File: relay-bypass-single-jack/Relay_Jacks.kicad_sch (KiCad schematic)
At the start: 14 parts, among them J1 4, J3 4, K1 IM05JR, Q1 DMN62D0U-7, U6 TLP170AM

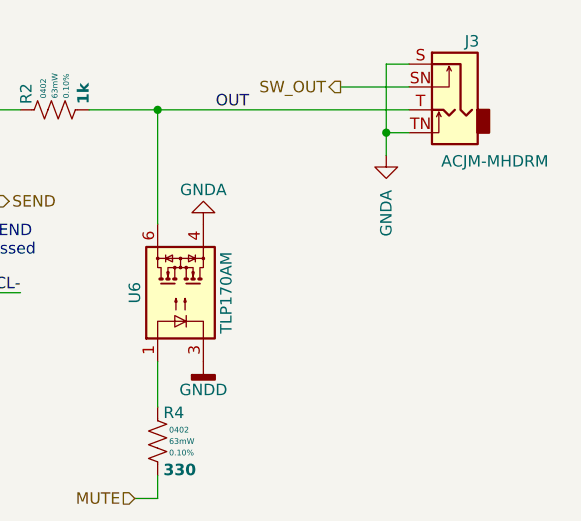
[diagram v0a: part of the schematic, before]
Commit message: Added second project for exploring a single-jack side mounted version
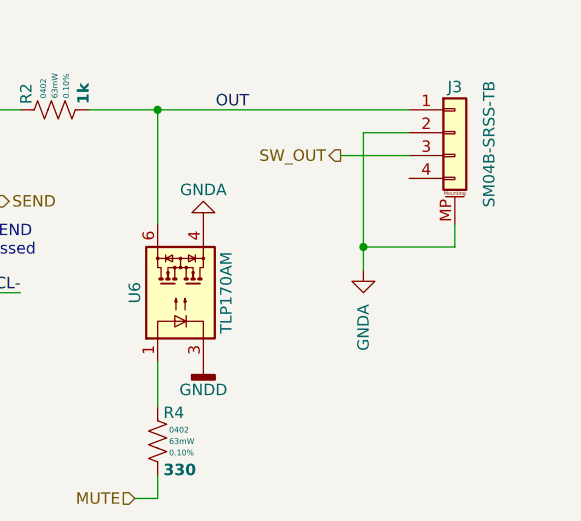
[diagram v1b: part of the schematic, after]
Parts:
- removed J3: 4, g-con:Amphenol_ACJM-MHDR(M), symbol #gplm:con/CON-1003-M301
- added J3: 4, Connector_JST:JST_SH_BM04B-SRSS-TB_1x04-1MP_P1.00mm_Vertical, symbol #gplm:con/CON-5001-0004
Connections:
- net GNDA: now also J3.2 (Pin_2), J3.MP (MountPin)
- net OUT: now also J3.1 (Pin_1)
- net SW_OUT: now also J3.3 (Pin_3)
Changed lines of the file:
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@@
 	)
 	(junction
-		(at 233.68 58.42)
-		(diameter 0)
-		(color 0 0 0 0)
-	)
-	(junction
 		(at 119.38 60.96)
 		(diameter 0)
@@
 	)
 	(junction
+		(at 231.14 71.12)
+		(diameter 0)
+		(color 0 0 0 0)
+	)
+	(junction
 		(at 152.4 76.2)
 		(diameter 0)
@@
 	(wire
 		(pts
-			(xy 233.68 60.96) (xy 233.68 58.42)
+			(xy 231.14 73.66) (xy 231.14 71.12)
 		)
 		(stroke
@@
 	(wire
 		(pts
+			(xy 241.3 68.58) (xy 241.3 71.12)
+		)
+		(stroke
+			(width 0)
+			(type default)
+		)
+	)
+	(wire
+		(pts
 			(xy 144.78 83.82) (xy 144.78 82.55)
 		)
@@
 	(wire
 		(pts
+			(xy 231.14 71.12) (xy 231.14 58.42)
+		)
+		(stroke
+			(width 0)
+			(type default)
+		)
+	)
+	(wire
+		(pts
 			(xy 163.83 116.84) (xy 170.18 116.84)
 		)
@@
 	(wire
 		(pts
-			(xy 236.22 53.34) (xy 228.6 53.34)
+			(xy 236.22 60.96) (xy 228.6 60.96)
 		)
 		(stroke
@@
 	(wire
 		(pts
-			(xy 233.68 58.42) (xy 236.22 58.42)
+			(xy 231.14 58.42) (xy 236.22 58.42)
 		)
 		(stroke
@@
 	(wire
 		(pts
-			(xy 182.88 111.76) (xy 182.88 116.84)
+			(xy 241.3 71.12) (xy 231.14 71.12)
 		)
 		(stroke
@@
 	(wire
 		(pts
-			(xy 116.84 53.34) (xy 119.38 53.34)
+			(xy 182.88 111.76) (xy 182.88 116.84)
 		)
 		(stroke
@@
 	(wire
 		(pts
-			(xy 165.1 63.5) (xy 162.56 63.5)
+			(xy 116.84 53.34) (xy 119.38 53.34)
 		)
 		(stroke
@@
 	(wire
 		(pts
-			(xy 208.28 55.88) (xy 236.22 55.88)
+			(xy 165.1 63.5) (xy 162.56 63.5)
 		)
 		(stroke
@@
 	(wire
 		(pts
-			(xy 233.68 50.8) (xy 233.68 58.42)
+			(xy 208.28 55.88) (xy 236.22 55.88)
 		)
 		(stroke
@@
 	(wire
 		(pts
-			(xy 236.22 50.8) (xy 233.68 50.8)
-		)
-		(stroke
-			(width 0)
-			(type default)
-		)
-	)
-	(wire
-		(pts
 			(xy 149.86 106.68) (xy 165.1 106.68)
 		)
@@
 	(hierarchical_label "SW_OUT"
 		(shape output)
-		(at 228.6 53.34 180)
+		(at 228.6 60.96 180)
 		(effects
 			(font
@@
 	)
 	(symbol
+		(lib_id "#gplm:con/CON-5001-0004")
+		(at 241.3 58.42 0)
+		(unit 1)
+		(exclude_from_sim no)
+		(in_bom yes)
+		(on_board yes)
+		(dnp no)
+		(property "Reference" "J3"
+			(at 241.3 53.34 0)
+			(effects
+				(font
+					(size 1.27 1.27)
+				)
+			)
+		)
+		(property "Value" "4"
+			(at 242.57 66.04 0)
+			(effects
+				(font
+					(size 1.27 1.27)
+				)
+				(justify left)
+				(hide yes)
+			)
+		)
+		(property "Footprint" "Connector_JST:JST_SH_BM04B-SRSS-TB_1x04-1MP_P1.00mm_Vertical"
+			(at 241.3 58.42 0)
+			(effects
+				(font
+					(size 1.27 1.27)
+				)
+				(hide yes)
+			)
+		)
+		(property "Datasheet" "https://www.jst.com/wp-content/uploads/2021/01/eSH-new.pdf"
+			(at 241.3 58.42 0)
+			(effects
+				(font
+					(size 1.27 1.27)
+				)
+				(hide yes)
+			)
+		)
+		(property "Description" "CONN WIRE TO BOARD SMD R/A 4POS 1MM"
+			(at 241.3 58.42 0)
+			(effects
+				(font
+					(size 1.27 1.27)
+				)
+				(hide yes)
+			)
+		)
+		(property "IPN" "CON-5001-0004"
+			(at 241.3 58.42 0)
+			(effects
+				(font
+					(size 1.27 1.27)
+				)
+				(hide yes)
+			)
+		)
+		(property "Manufacturer" "JST"
+			(at 241.3 58.42 0)
+			(effects
+				(font
+					(size 1.27 1.27)
+				)
+				(hide yes)
+			)
+		)
+		(property "MPN" "SM04B-SRSS-TB"
+			(at 245.11 59.69 90)
+			(effects
+				(font
+					(size 1.27 1.27)
+				)
+			)
+		)
+		(property "Pins" "4"
+			(at 241.3 58.42 0)
+			(effects
+				(font
+					(size 1.27 1.27)
+				)
+				(hide yes)
+			)
+		)
+		(pin "3"
+		)
+		(pin "4"
+		)
+		(pin "1"
+		)
+		(pin "2"
+		)
+		(pin "MP"
+		)
+		(instances
+			(project "relay-bypass-single-jack"
+				(path "/1a8abc1e-f066-401c-b73c-6efc7ca39ffd/0d11fddd-a8d6-4ffc-902f-d64a5c05d413"
+					(reference "J3")
+					(unit 1)
+				)
+			)
+		)
+	)
+	(symbol
 		(lib_id "power:GNDD")
 		(at 152.4 88.9 0)
@@
 	)
 	(symbol
-		(lib_id "#gplm:con/CON-1003-M301")
-		(at 241.3 55.88 0)
-		(mirror y)
-		(unit 1)
-		(exclude_from_sim no)
-		(in_bom yes)
-		(on_board yes)
-		(dnp no)
-		(property "Reference" "J3"
-			(at 243.205 48.26 0)
-			(effects
-				(font
-					(size 1.27 1.27)
-				)
-			)
-		)
-		(property "Value" "4"
-			(at 241.3 46.99 0)
-			(effects
-				(font
-					(size 1.27 1.27)
-				)
-				(hide yes)
-			)
-		)
-		(property "Footprint" "g-con:Amphenol_ACJM-MHDR(M)"
-			(at 241.3 50.8 0)
-			(effects
-				(font
-					(size 1.27 1.27)
-				)
-				(hide yes)
-			)
-		)
-		(property "Datasheet" ""
-			(at 241.3 50.8 0)
-			(effects
-				(font
-					(size 1.27 1.27)
-				)
-				(hide yes)
-			)
-		)
-		(property "Description" "¼ in Audio Jack, TS, NC switch x2, Outtie, Low Profile, Metal shaft, metal  threads"
-			(at 241.3 55.88 0)
-			(effects
-				(font
-					(size 1.27 1.27)
-				)
-				(hide yes)
-			)
-		)
-		(property "IPN" "CON-1003-M301"
-			(at 241.3 55.88 0)
-			(effects
-				(font
-					(size 1.27 1.27)
-				)
-				(hide yes)
-			)
-		)
-		(property "Manufacturer" "Amphenol Audio"
-			(at 241.3 55.88 0)
-			(effects
-				(font
-					(size 1.27 1.27)
-				)
-				(hide yes)
-			)
-		)
-		(property "MPN" "ACJM-MHDRM"
-			(at 245.745 61.595 0)
-			(effects
-				(font
-					(size 1.27 1.27)
-				)
-			)
-		)
-		(property "Pins" "4"
-			(at 241.3 55.88 0)
-			(effects
-				(font
-					(size 1.27 1.27)
-				)
-				(hide yes)
-			)
-		)
-		(pin "TN"
-		)
-		(pin "S"
-		)
-		(pin "T"
-		)
-		(pin "SN"
-		)
-		(instances
-			(project "relay-bypass"
-				(path "/1a8abc1e-f066-401c-b73c-6efc7ca39ffd/0d11fddd-a8d6-4ffc-902f-d64a5c05d413"
-					(reference "J3")
-					(unit 1)
-				)
-			)
-		)
-	)
-	(symbol
 		(lib_id "#gplm:cap/CAP-4103-100N")
 		(at 163.83 124.46 0)
@@
 	(symbol
 		(lib_id "power:GNDA")
-		(at 233.68 60.96 0)
+		(at 231.14 73.66 0)
 		(unit 1)
 		(exclude_from_sim no)
@@
 		(fields_autoplaced yes)
 		(property "Reference" "#PWR029"
-			(at 233.68 67.31 0)
+			(at 231.14 80.01 0)
 			(effects
 				(font
@@
 		)
 		(property "Value" "GNDA"
-			(at 233.6801 64.77 90)
+			(at 231.1401 77.47 90)
 			(effects
 				(font
@@
 		)
 		(property "Footprint" ""
-			(at 233.68 60.96 0)
+			(at 231.14 73.66 0)
 			(effects
 				(font
@@
 		)
 		(property "Datasheet" ""
-			(at 233.68 60.96 0)
+			(at 231.14 73.66 0)
 			(effects
 				(font
@@
 		)
 		(property "Description" "Power symbol creates a global label with name \"GNDA\" , analog ground"
-			(at 233.68 60.96 0)
+			(at 231.14 73.66 0)
 			(effects
 				(font

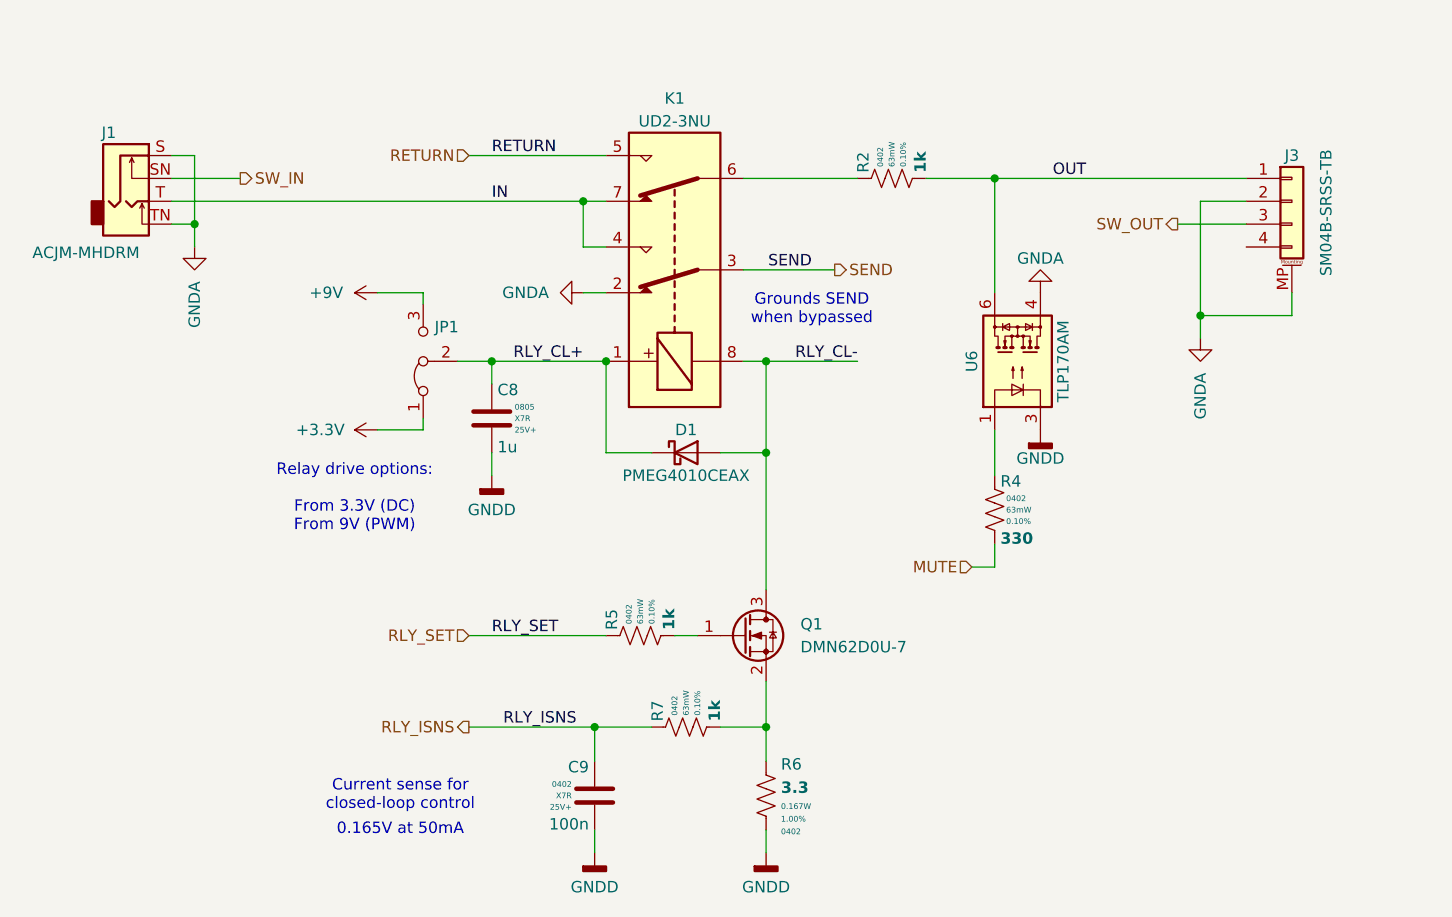
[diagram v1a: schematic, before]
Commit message: Pivoted to dual-jack version on opposing sides.
125B only, using "innie" jacks. Solder-in-place.
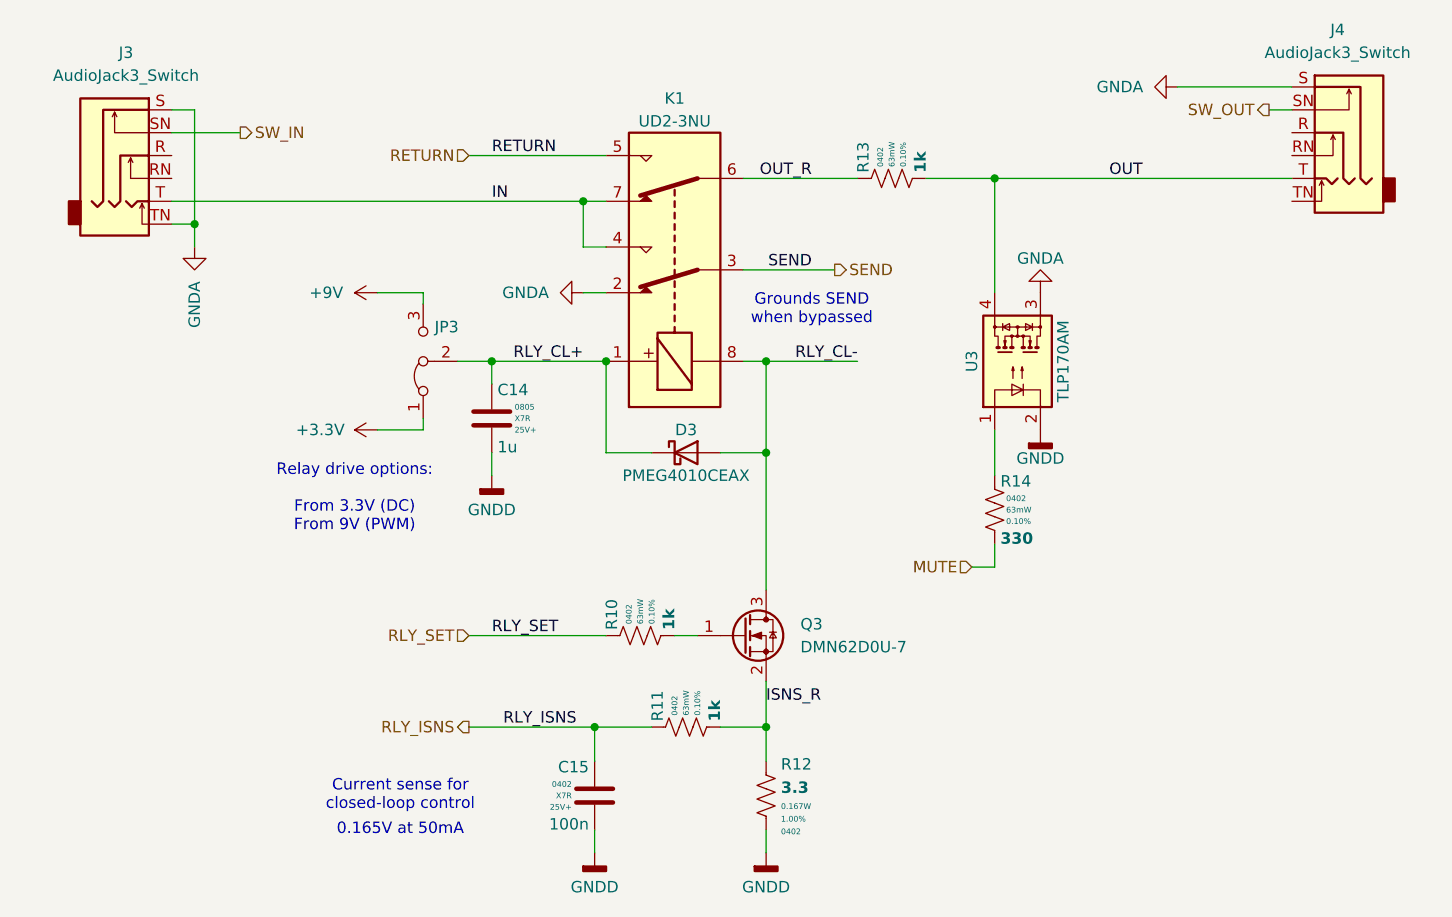
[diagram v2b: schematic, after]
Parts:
- removed J1: 4, g-con:Amphenol_ACJM-MHDR(M), symbol #gplm:con/CON-1003-M301
- removed J3: 4, Connector_JST:JST_SH_BM04B-SRSS-TB_1x04-1MP_P1.00mm_Vertical, symbol #gplm:con/CON-5001-0004
- added J3, J4: AudioJack3_Switch, g-con:Jack_6.35mm_Neutrik_NMJ6HCD2_LARGE_SLOTS, symbol Connector_Audio:AudioJack3_Switch
- renumbered C8 to C14, C9 to C15, D1 to D3, JP1 to JP3, Q1 to Q3, R5 to R10, R7 to R11, R6 to R12, R2 to R13, R4 to R14, U6 to U3
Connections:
- net GNDA: now also U3.3, J3.S, J3.TN, J4.S; no longer U3.4
- net GNDD: now also U3.2; no longer U3.3
- net IN: now also J3.T
- net OUT: now also U3.4, J4.T; no longer U3.6
- net SW_IN: now also J3.SN
- net SW_OUT: now also J4.SN
- net OUT_R: now reaches K1.6, R13.1
- net ISNS_R: now reaches Q3.2 (S), R11.2, R12.1
